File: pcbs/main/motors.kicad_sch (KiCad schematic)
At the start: 36 parts, among them Q1 2SC945, Q2 2SC945, Q3 2SC945, Q4 2SC945, Q5 2SC945, Q6 2SC945, Q7 2SC945, Q8 2SC945

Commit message: Edits for custom board
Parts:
- removed R1, R13, R19, R7: 22k, PCM_Resistor_THT_AKL:R_Axial_DIN0207_L6.3mm_D2.5mm_P7.62mm_Horizontal, symbol Device:R_US
- removed R14, R2, R20, R8: 3.3k, PCM_Resistor_THT_AKL:R_Axial_DIN0207_L6.3mm_D2.5mm_P7.62mm_Horizontal, symbol Device:R_US
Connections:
- no-connect marks 0 -> 4

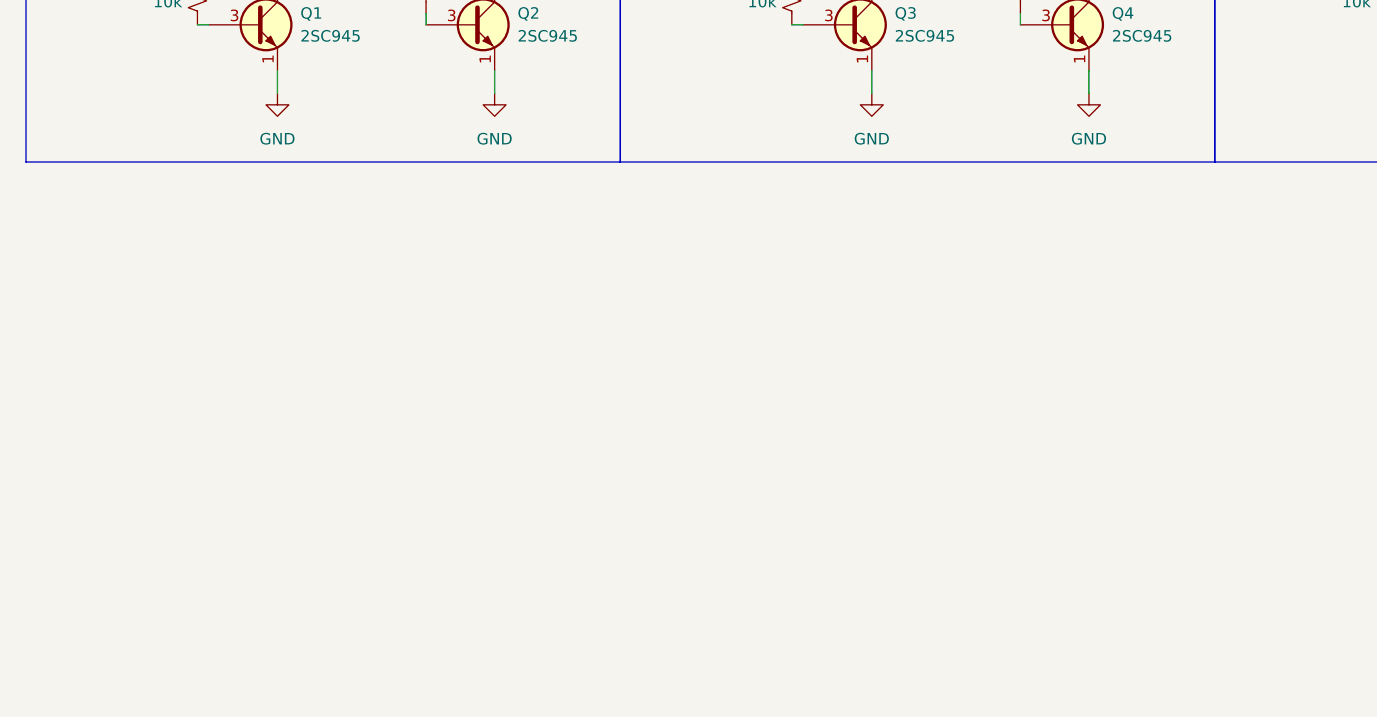
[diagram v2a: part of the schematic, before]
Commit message: feat: radio and motor encoders
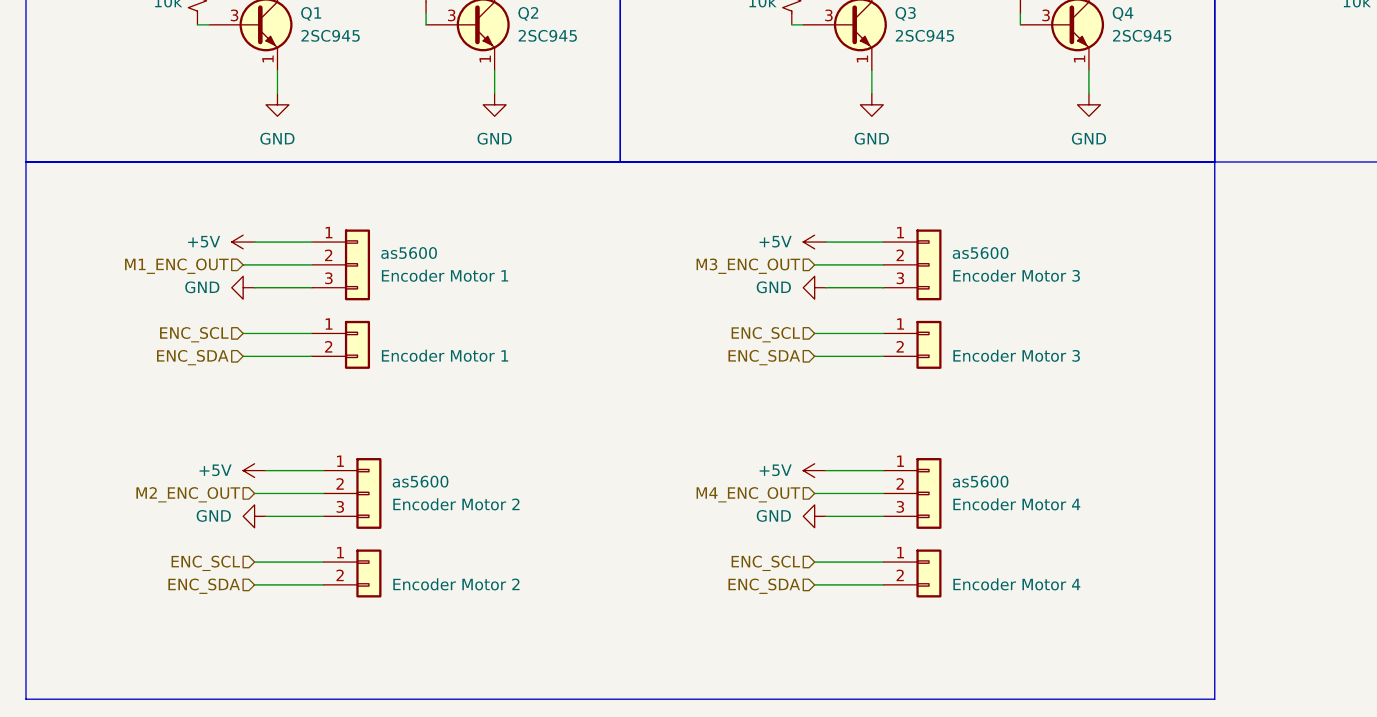
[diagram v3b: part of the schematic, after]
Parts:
- added as2: Encoder Motor 3, symbol Connector_Generic:Conn_01x02
- added as4: Encoder Motor 2, symbol Connector_Generic:Conn_01x02
- added as5600: Encoder Motor 2, symbol Connector_Generic:Conn_01x03
- added as5600: Encoder Motor 1, symbol Connector_Generic:Conn_01x02
- added as5600: Encoder Motor 1, symbol Connector_Generic:Conn_01x03
- added as5600: Encoder Motor 3, symbol Connector_Generic:Conn_01x03
- added as5600: Encoder Motor 4, symbol Connector_Generic:Conn_01x03
- added as6: Encoder Motor 4, symbol Connector_Generic:Conn_01x02
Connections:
- net +5V: now also as5600.1 (Pin_1), as5600.1 (Pin_1), as5600.1 (Pin_1), as5600.1 (Pin_1)
- net GND: now also as5600.3 (Pin_3), as5600.3 (Pin_3), as5600.3 (Pin_3), as5600.3 (Pin_3)
- new net ENC_SCL: as2.1 (Pin_1), as4.1 (Pin_1), as5600.1 (Pin_1), as6.1 (Pin_1)
- new net ENC_SDA: as2.2 (Pin_2), as4.2 (Pin_2), as5600.2 (Pin_2), as6.2 (Pin_2)
- new net M1_ENC_OUT: as5600.2 (Pin_2)
- new net M2_ENC_OUT: as5600.2 (Pin_2)
- new net M3_ENC_OUT: as5600.2 (Pin_2)
- new net M4_ENC_OUT: as5600.2 (Pin_2)

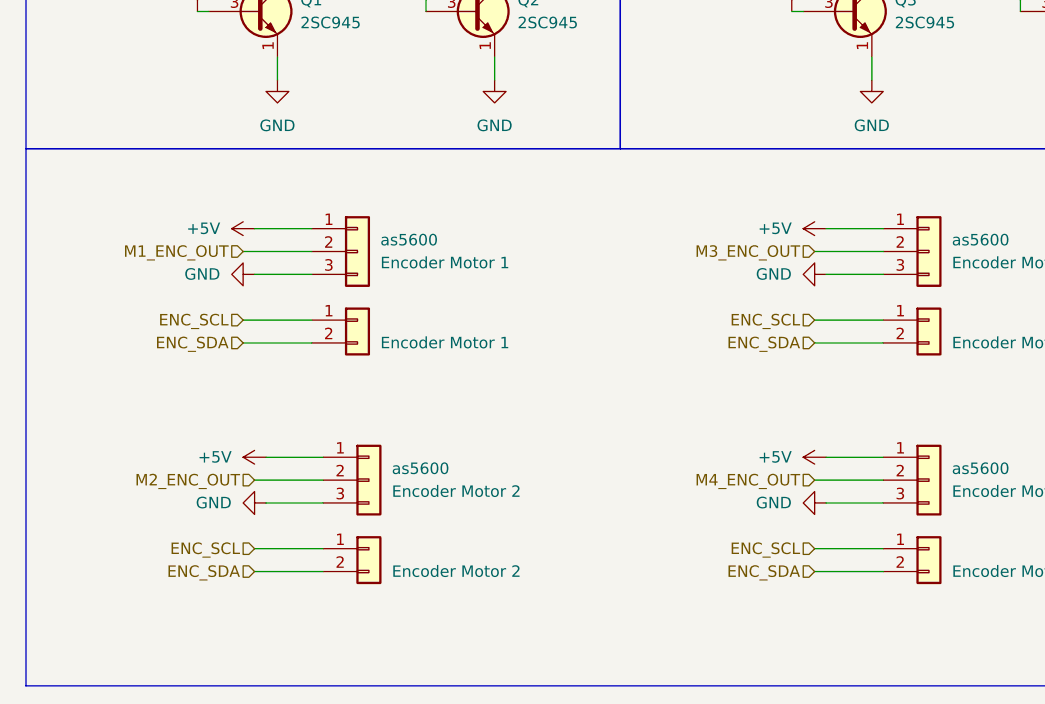
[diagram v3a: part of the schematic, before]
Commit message: fea: add jumpers to I2C encoders config
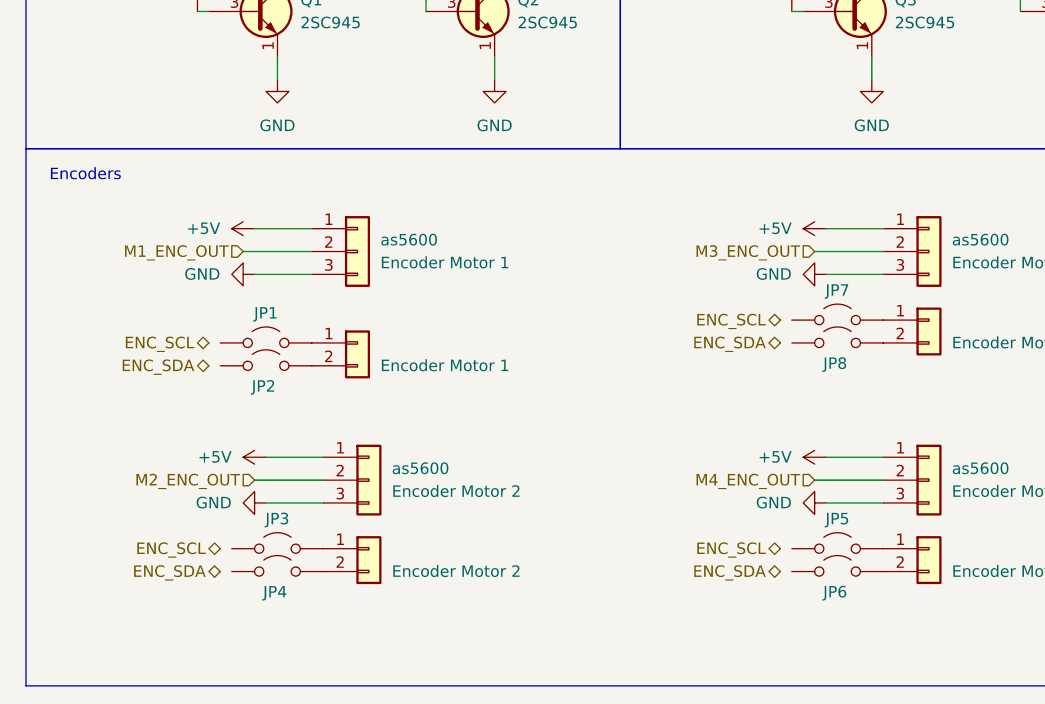
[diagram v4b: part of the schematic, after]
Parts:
- added JP1, JP2, JP3, JP4, JP5, JP6, JP7, JP8: Jumper_2_Open, symbol Jumper:Jumper_2_Open
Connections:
- net ENC_SCL: no longer as2.1 (Pin_1), as4.1 (Pin_1), as5600.1 (Pin_1), as6.1 (Pin_1)
- net ENC_SDA: no longer as2.2 (Pin_2), as4.2 (Pin_2), as5600.2 (Pin_2), as6.2 (Pin_2)
- new net: JP5.2 (B), as6.1 (Pin_1)
- new net: JP6.2 (B), as6.2 (Pin_2)
- new net: JP8.2 (B), as2.2 (Pin_2)
- new net: JP4.2 (B), as4.2 (Pin_2)
- new net: JP1.2 (B), as5600.1 (Pin_1)
- new net: JP2.2 (B), as5600.2 (Pin_2)
- new net: JP7.2 (B), as2.1 (Pin_1)
- new net: JP3.2 (B), as4.1 (Pin_1)
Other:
- note added: "Encoders"

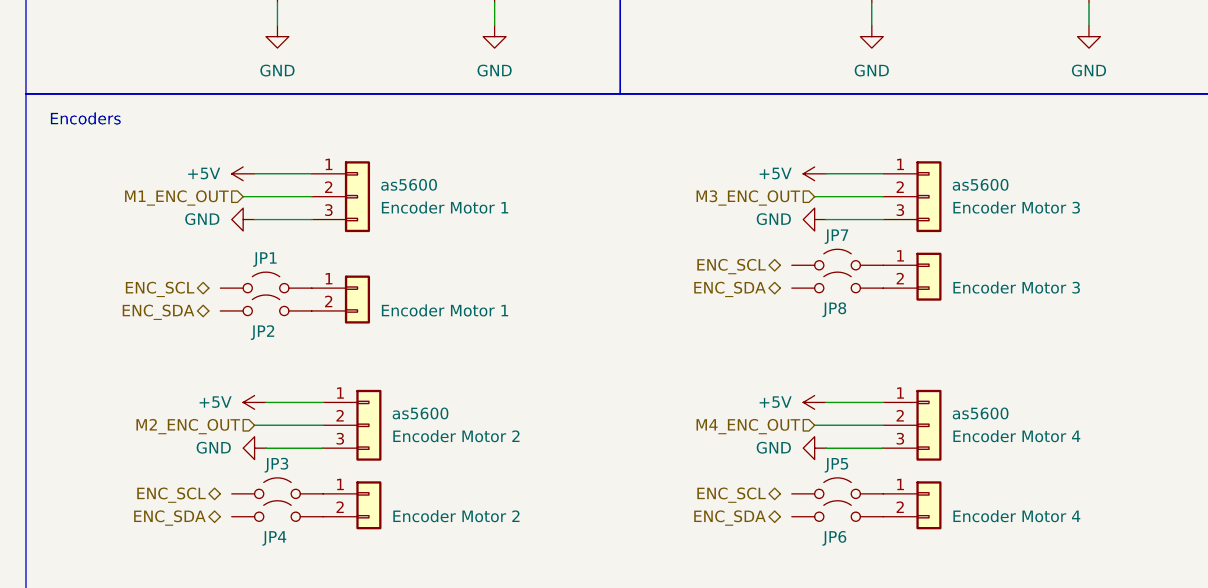
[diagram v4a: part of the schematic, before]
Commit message: wip: change radio footprint
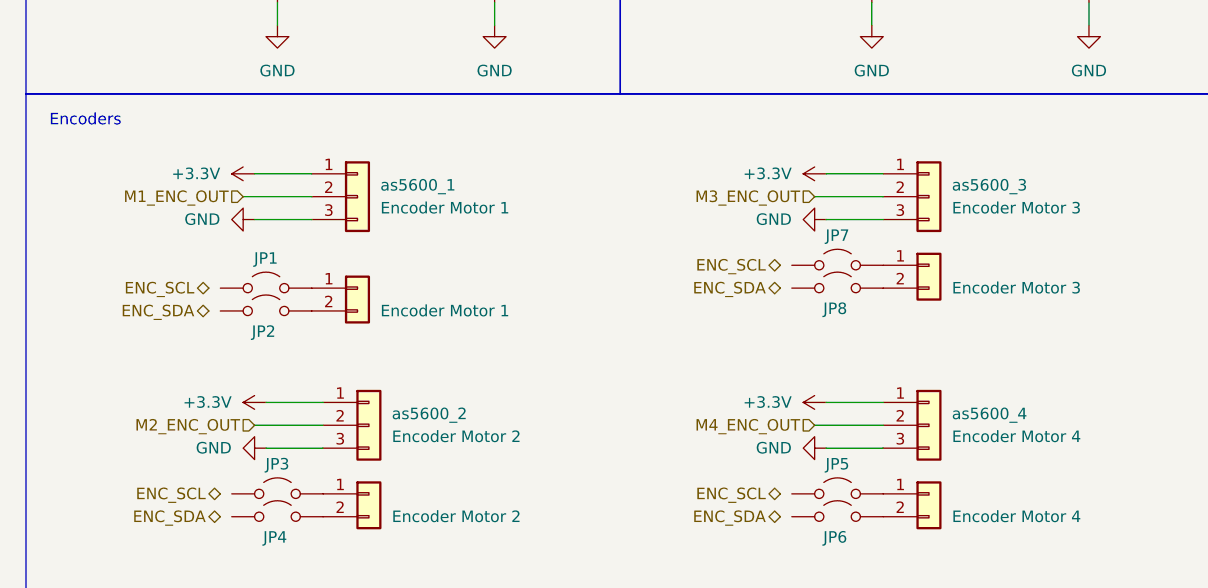
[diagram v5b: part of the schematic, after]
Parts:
- renumbered as5600 to as5600_1, as5600 to as5600_2, as5600 to as5600_3, as5600 to as5600_4
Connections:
- net +5V: no longer as5600_1.1 (Pin_1), as5600_2.1 (Pin_1), as5600_3.1 (Pin_1), as5600_4.1 (Pin_1)
- new net +3.3V: as5600_1.1 (Pin_1), as5600_2.1 (Pin_1), as5600_3.1 (Pin_1), as5600_4.1 (Pin_1)

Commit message: feat: association of footprints
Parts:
- JP1, JP2, JP3, JP4, JP5, JP6, JP7, JP8: footprint (none) -> Jumper:SolderJumper-2_P1.3mm_Bridged2Bar_Pad1.0x1.5mm
- as2, as4, as5600, as6: footprint (none) -> Connector_JST:JST_ACH_BM02B-ACHSS-GAN-ETF_1x02-1MP_P1.20mm_Vertical
- as5600_1, as5600_2, as5600_3, as5600_4: footprint (none) -> Connector_JST:JST_ACH_BM03B-ACHSS-GAN-ETF_1x03-1MP_P1.20mm_Vertical
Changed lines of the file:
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@@
 			)
 		)
-		(property "Footprint" ""
+		(property "Footprint" "Jumper:SolderJumper-2_P1.3mm_Bridged2Bar_Pad1.0x1.5mm"
 			(at 106.68 176.53 0)
 			(effects
@@
 			)
 		)
-		(property "Footprint" ""
+		(property "Footprint" "Connector_JST:JST_ACH_BM02B-ACHSS-GAN-ETF_1x02-1MP_P1.20mm_Vertical"
 			(at 116.84 176.53 0)
 			(effects
@@
 			)
 		)
-		(property "Footprint" ""
+		(property "Footprint" "Connector_JST:JST_ACH_BM03B-ACHSS-GAN-ETF_1x03-1MP_P1.20mm_Vertical"
 			(at 54.61 168.91 0)
 			(effects
@@
 			)
 		)
-		(property "Footprint" ""
+		(property "Footprint" "Jumper:SolderJumper-2_P1.3mm_Bridged2Bar_Pad1.0x1.5mm"
 			(at 106.68 153.67 0)
 			(effects
@@
 			)
 		)
-		(property "Footprint" ""
+		(property "Footprint" "Jumper:SolderJumper-2_P1.3mm_Bridged2Bar_Pad1.0x1.5mm"
 			(at 44.45 179.07 0)
 			(effects
@@
 			)
 		)
-		(property "Footprint" ""
+		(property "Footprint" "Jumper:SolderJumper-2_P1.3mm_Bridged2Bar_Pad1.0x1.5mm"
 			(at 43.18 153.67 0)
 			(effects
@@
 			)
 		)
-		(property "Footprint" ""
+		(property "Footprint" "Connector_JST:JST_ACH_BM02B-ACHSS-GAN-ETF_1x02-1MP_P1.20mm_Vertical"
 			(at 53.34 153.67 0)
 			(effects
@@
 			)
 		)
-		(property "Footprint" ""
+		(property "Footprint" "Jumper:SolderJumper-2_P1.3mm_Bridged2Bar_Pad1.0x1.5mm"
 			(at 106.68 151.13 0)
 			(effects
@@
 			)
 		)
-		(property "Footprint" ""
+		(property "Footprint" "Connector_JST:JST_ACH_BM02B-ACHSS-GAN-ETF_1x02-1MP_P1.20mm_Vertical"
 			(at 54.61 176.53 0)
 			(effects
@@
 			)
 		)
-		(property "Footprint" ""
+		(property "Footprint" "Jumper:SolderJumper-2_P1.3mm_Bridged2Bar_Pad1.0x1.5mm"
 			(at 43.18 156.21 0)
 			(effects
@@
 			)
 		)
-		(property "Footprint" ""
+		(property "Footprint" "Connector_JST:JST_ACH_BM02B-ACHSS-GAN-ETF_1x02-1MP_P1.20mm_Vertical"
 			(at 116.84 151.13 0)
 			(effects
@@
 			)
 		)
-		(property "Footprint" ""
+		(property "Footprint" "Connector_JST:JST_ACH_BM03B-ACHSS-GAN-ETF_1x03-1MP_P1.20mm_Vertical"
 			(at 53.34 143.51 0)
 			(effects
@@
 			)
 		)
-		(property "Footprint" ""
+		(property "Footprint" "Connector_JST:JST_ACH_BM03B-ACHSS-GAN-ETF_1x03-1MP_P1.20mm_Vertical"
 			(at 116.84 143.51 0)
 			(effects
@@
 			)
 		)
-		(property "Footprint" ""
+		(property "Footprint" "Jumper:SolderJumper-2_P1.3mm_Bridged2Bar_Pad1.0x1.5mm"
 			(at 106.68 179.07 0)
 			(effects
@@
 			)
 		)
-		(property "Footprint" ""
+		(property "Footprint" "Jumper:SolderJumper-2_P1.3mm_Bridged2Bar_Pad1.0x1.5mm"
 			(at 44.45 176.53 0)
 			(effects
@@
 			)
 		)
-		(property "Footprint" ""
+		(property "Footprint" "Connector_JST:JST_ACH_BM03B-ACHSS-GAN-ETF_1x03-1MP_P1.20mm_Vertical"
 			(at 116.84 168.91 0)
 			(effects
